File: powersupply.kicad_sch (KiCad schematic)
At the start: 13 parts, among them U1 MAX604

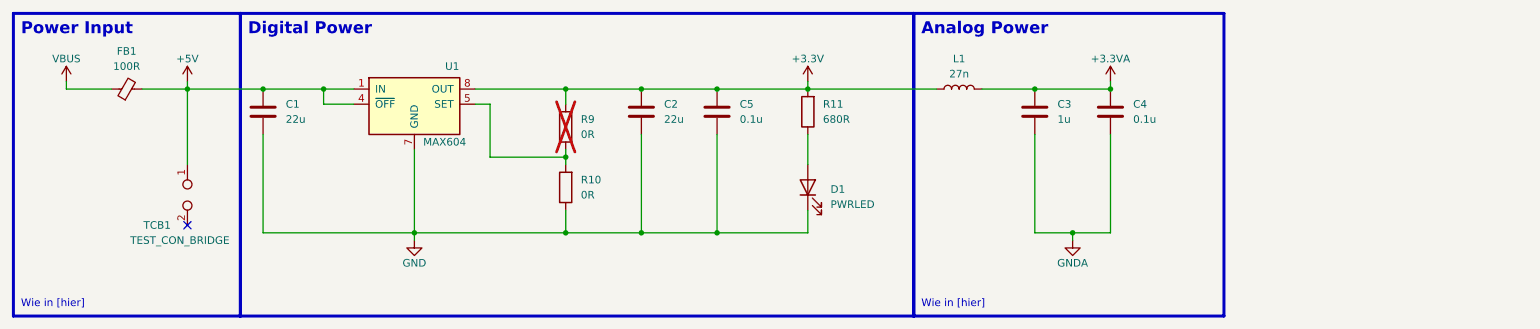
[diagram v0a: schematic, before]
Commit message: Added ESD, updated Footprints, BOM, etc.
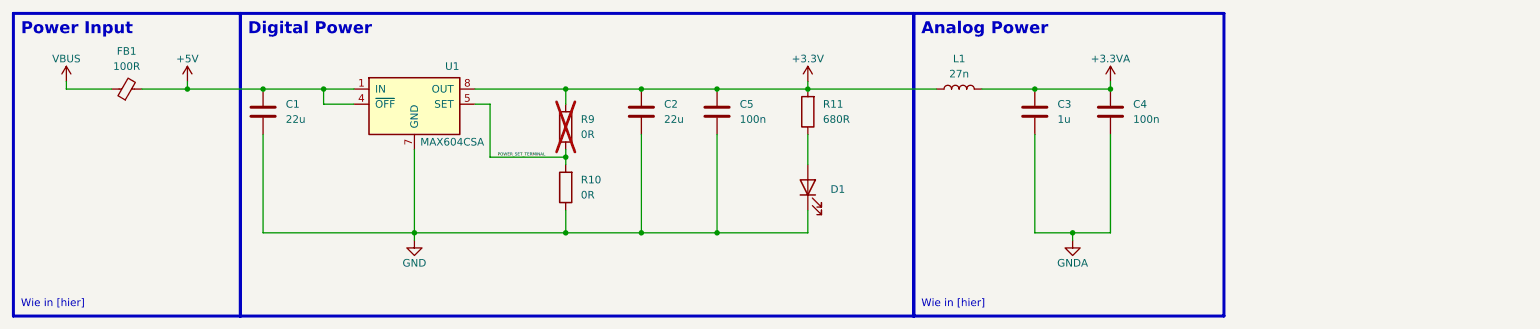
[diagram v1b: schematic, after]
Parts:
- removed TCB1: TEST_CON_BRIDGE, Jumper:SolderJumper-2_P1.3mm_Bridged_Pad1.0x1.5mm, symbol Connector:TestPoint_2Pole
- C4, C5: value 0.1u -> 100n
- D1: value PWRLED -> SML-LX0402UPGC-TR
- U1: value MAX604 -> MAX604CSA
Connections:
- net POWER_SET_TERMINAL: now reaches R10.2, R9.1, U1.5 (SET)
- no-connect marks 1 -> 0
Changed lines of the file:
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@@
   (junction (at 130.81 38.1) (diameter 0) (color 0 0 0 0)
   )
-  (no_connect (at 54.61 60.96))
   (wire (pts (xy 92.71 63.5) (xy 92.71 62.23))
     (stroke (width 0) (type default))
@@
   )
   (wire (pts (xy 54.61 38.1) (xy 67.31 38.1))
-    (stroke (width 0) (type default))
-  )
-  (wire (pts (xy 54.61 38.1) (xy 54.61 50.8))
     (stroke (width 0) (type default))
   )
@@
     (effects (font (size 2 2) (thickness 0.254) bold (color 100 100 100 1)) (justify left bottom))
   )
+  (label "POWER_SET_TERMINAL" (at 106.68 49.53 0) (fields_autoplaced)
+    (effects (font (size 0.5 0.5)) (justify left bottom))
+    (property "Netclass" "Power" (at 106.68 50.03 0)
+      (effects (font (size 0.5 0.5) italic) (justify left))
+    )
+  )
   (symbol (lib_id "Device:C") (at 209.55 41.91 0) (unit 1)
     (in_bom yes) (on_board yes) (dnp no) (fields_autoplaced)
@@
       (effects (font (size 1.27 1.27)) (justify left))
     )
-    (property "Value" "0.1u" (at 213.36 43.18 0)
+    (property "Value" "100n" (at 213.36 43.18 0)
       (effects (font (size 1.27 1.27)) (justify left))
     )
@@
       (effects (font (size 1.27 1.27)) hide)
     )
-    (property "Datasheet" "https://www.mouser.de/datasheet/2/40/AutoMLCCKAM-3216307.pdf" (at 209.55 41.91 0)
+    (property "Datasheet" "~" (at 209.55 41.91 0)
       (effects (font (size 1.27 1.27)) hide)
     )
@@
       (effects (font (size 1.27 1.27)) hide)
     )
-    (property "Datasheet" "https://www.mouser.de/datasheet/2/447/EMI-3217982.pdf" (at 44.45 38.1 0)
+    (property "Datasheet" "~" (at 44.45 38.1 0)
       (effects (font (size 1.27 1.27)) hide)
     )
@@
       (effects (font (size 1.27 1.27)) (justify left))
     )
-    (property "Value" "0.1u" (at 147.32 43.18 0)
+    (property "Value" "100n" (at 147.32 43.18 0)
       (effects (font (size 1.27 1.27)) (justify left))
     )
@@
       (effects (font (size 1.27 1.27)) hide)
     )
-    (property "Datasheet" "https://www.mouser.de/datasheet/2/40/AutoMLCCKAM-3216307.pdf" (at 143.51 41.91 0)
+    (property "Datasheet" "~" (at 143.51 41.91 0)
       (effects (font (size 1.27 1.27)) hide)
     )
@@
       (effects (font (size 1.27 1.27)) hide)
     )
-    (property "Datasheet" "https://www.mouser.de/datasheet/2/40/AutoMLCCKAM-3216307.pdf" (at 67.31 41.91 0)
+    (property "Datasheet" "~" (at 67.31 41.91 0)
       (effects (font (size 1.27 1.27)) hide)
     )
@@
       (effects (font (size 1.27 1.27)) hide)
     )
-    (property "Datasheet" "https://www.mouser.de/datasheet/2/40/AutoMLCCKAM-3216307.pdf" (at 130.81 41.91 0)
+    (property "Datasheet" "~" (at 130.81 41.91 0)
       (effects (font (size 1.27 1.27)) hide)
     )
@@
       (effects (font (size 1.27 1.27)) hide)
     )
-    (property "Datasheet" "https://www.mouser.de/datasheet/2/40/AutoMLCCKAM-3216307.pdf" (at 196.85 41.91 0)
+    (property "Datasheet" "~" (at 196.85 41.91 0)
       (effects (font (size 1.27 1.27)) hide)
     )
@@
       (effects (font (size 1.27 1.27)))
     )
-    (property "Value" "MAX604" (at 97.79 46.99 0)
+    (property "Value" "MAX604CSA" (at 99.06 46.99 0)
       (effects (font (size 1.27 1.27)))
     )
@@
       (effects (font (size 1.27 1.27)) (justify right))
     )
-    (property "Value" "PWRLED" (at 162.56 57.4675 90)
-      (effects (font (size 1.27 1.27)) (justify right))
+    (property "Value" "SML-LX0402UPGC-TR" (at 162.56 57.4675 90)
+      (effects (font (size 1.27 1.27)) (justify right) hide)
     )
     (property "Footprint" "LED_SMD:LED_0402_1005Metric" (at 158.75 54.61 0)
       (effects (font (size 1.27 1.27)) hide)
     )
-    (property "Datasheet" "https://www.mouser.de/datasheet/2/244/LUMX_S_A0003328320_1-2552030.pdf" (at 158.75 54.61 0)
+    (property "Datasheet" "~" (at 158.75 54.61 0)
       (effects (font (size 1.27 1.27)) hide)
     )
@@
         )
       )
-    )
-  )
-  (symbol (lib_id "Connector:TestPoint_2Pole") (at 54.61 55.88 270) (unit 1)
-    (in_bom yes) (on_board yes) (dnp no)
-    (property "Reference" "TCB1" (at 49.53 60.96 90)
-      (effects (font (size 1.27 1.27)))
-    )
-    (property "Value" "TEST_CON_BRIDGE" (at 53.34 63.5 90)
-      (effects (font (size 1.27 1.27)))
-    )
-    (property "Footprint" "Jumper:SolderJumper-2_P1.3mm_Bridged_Pad1.0x1.5mm" (at 54.61 55.88 0)
-      (effects (font (size 1.27 1.27)) hide)
-    )
-    (property "Datasheet" "~" (at 54.61 55.88 0)
-      (effects (font (size 1.27 1.27)) hide)
-    )
-    (pin "1")
-    (pin "2")
-    (instances
-      (project "schneidbrett"
-        (path "/c05974a1-d9e7-44bd-b1f3-81c4ede4353c/86ba3294-cf4a-47ab-b34c-9be2b0ce2123"
-          (reference "TCB1") (unit 1)
-        )
-      )

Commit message: Schematic is done for now, starting layout
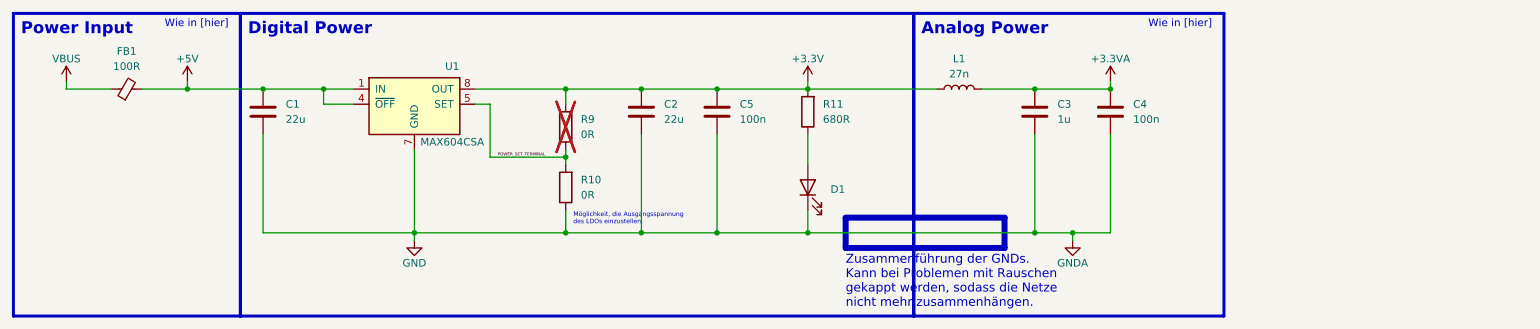
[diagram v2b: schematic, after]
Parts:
- D1: Distributor Link (none) -> https://www.mouser.de/ProductDetail/Lumex/SML-LX0402UPGC-TR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; MFN SML-LX0402UPGC-TR -> (none); Manufacturer (none) -> Lumex; Manufacturer Number (none) -> SML-LX0402UPGC-TR
- FB1: Distributor Link (none) -> https://www.mouser.de/ProductDetail/Pulse-Electronics/BBUP0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; MFN BBUP00321611101Y00 -> (none); Manufacturer (none) -> Pulse Electronics; Manufacturer Number (none) -> BBUP00321611101Y00
- U1: Distributor Link (none) -> https://www.mouser.de/ProductDetail/Analog-Devices-Maxim-In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; MFN MAX604CSA -> (none); Manufacturer (none) -> Analog Devices / Maxim Integrated; Manufacturer Number (none) -> MAX604CSA+
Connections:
- net GNDA is gone; now on net GND: C3.2, C4.2
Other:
- note added: "Möglichkeit, die Ausgangsspannung des LDOs einzustellen."
- note added: "Zusammenführung der GNDs. Kann bei Problemen mit Rauschen gekappt werden, sodass die Netze nicht mehr zusammenhängen."
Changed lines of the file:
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@@
   (junction (at 196.85 38.1) (diameter 0) (color 0 0 0 0)
   )
+  (junction (at 158.75 62.23) (diameter 0) (color 0 0 0 0)
+  )
   (junction (at 77.47 38.1) (diameter 0) (color 0 0 0 0)
   )
@@
   (junction (at 130.81 38.1) (diameter 0) (color 0 0 0 0)
   )
+  (junction (at 196.85 62.23) (diameter 0) (color 0 0 0 0)
+  )
   (wire (pts (xy 92.71 63.5) (xy 92.71 62.23))
     (stroke (width 0) (type default))
@@
   )
   (wire (pts (xy 130.81 38.1) (xy 143.51 38.1))
+    (stroke (width 0) (type default))
+  )
+  (wire (pts (xy 158.75 62.23) (xy 196.85 62.23))
     (stroke (width 0) (type default))
   )
@@
     (fill (type none))
   )
+  (rectangle (start 165.1 59.69) (end 191.77 64.77)
+    (stroke (width 1) (type default) (color 229 0 0 1))
+    (fill (type none))
+  )
   (rectangle (start 176.53 25.4) (end 228.6 76.2)
     (stroke (width 0.5) (type default) (color 100 100 100 1))
     (fill (type none))
   )
-  (text "Wie in [hier]" (at 26.67 74.93 0)
+  (text "Wie in [hier]" (at 50.8 27.94 0)
     (effects (font (size 1.27 1.27)) (justify left bottom) (href "https://youtu.be/wLwKgMBWhpY?t=174"))
   )
-  (text "Wie in [hier]" (at 177.8 74.93 0)
+  (text "Möglichkeit, die Ausgangsspannung\ndes LDOs einzustellen."
+    (at 119.38 60.96 0)
+    (effects (font (size 0.75 0.75) (color 0 0 0 1)) (justify left bottom))
+  )
+  (text "Wie in [hier]" (at 215.9 27.94 0)
     (effects (font (size 1.27 1.27)) (justify left bottom) (href "https://youtu.be/wLwKgMBWhpY?t=214"))
+  )
+  (text "Zusammenführung der GNDs. \nKann bei Problemen mit Rauschen\ngekappt werden, sodass die Netze \nnicht mehr zusammenhängen."
+    (at 165.1 74.93 0)
+    (effects (font (size 1.5 1.5) (color 0 0 0 1)) (justify left bottom))
   )
   (text "Power Input" (at 26.67 29.21 0)
@@
       (effects (font (size 1.27 1.27)) hide)
     )
+    (property "Distributor Link" "" (at 209.55 41.91 0)
+      (effects (font (size 1.27 1.27)) hide)
+    )
+    (property "Manufacturer" "" (at 209.55 41.91 0)
+      (effects (font (size 1.27 1.27)) hide)
+    )
     (pin "1")
     (pin "2")
@@
       (effects (font (size 1.27 1.27)) hide)
     )
-    (property "MFN" "BBUP00321611101Y00" (at 44.45 38.1 90)
+    (property "Manufacturer Number" "BBUP00321611101Y00" (at 44.45 38.1 90)
+      (effects (font (size 1.27 1.27)) hide)
+    )
+    (property "Distributor Link" "https://www.mouser.de/ProductDetail/Pulse-Electronics/BBUP00321611101Y00?qs=rSMjJ%252B1ewcQLINSPAxGW4A%3D%3D" (at 44.45 38.1 0)
+      (effects (font (size 1.27 1.27)) hide)
+    )
+    (property "Manufacturer" "Pulse Electronics" (at 44.45 38.1 0)
       (effects (font (size 1.27 1.27)) hide)
     )
@@
     )
     (property "Datasheet" "~" (at 143.51 41.91 0)
+      (effects (font (size 1.27 1.27)) hide)
+    )
+    (property "Distributor Link" "" (at 143.51 41.91 0)
+      (effects (font (size 1.27 1.27)) hide)
+    )
+    (property "Manufacturer" "" (at 143.51 41.91 0)
       (effects (font (size 1.27 1.27)) hide)
     )
@@
       (effects (font (size 1.27 1.27)) hide)
     )
+    (property "Distributor Link" "" (at 118.11 44.45 0)
+      (effects (font (size 1.27 1.27)) hide)
+    )
+    (property "Manufacturer" "" (at 118.11 44.45 0)
+      (effects (font (size 1.27 1.27)) hide)
+    )
     (pin "1")
     (pin "2")
@@
       (effects (font (size 1.27 1.27)) hide)
     )
+    (property "Distributor Link" "" (at 118.11 54.61 0)
+      (effects (font (size 1.27 1.27)) hide)
+    )
+    (property "Manufacturer" "" (at 118.11 54.61 0)
+      (effects (font (size 1.27 1.27)) hide)
+    )
     (pin "1")
     (pin "2")
@@
       (effects (font (size 1.27 1.27)) hide)
     )
+    (property "Distributor Link" "" (at 67.31 41.91 0)
+      (effects (font (size 1.27 1.27)) hide)
+    )
+    (property "Manufacturer" "" (at 67.31 41.91 0)
+      (effects (font (size 1.27 1.27)) hide)
+    )
     (pin "1")
     (pin "2")
@@
     )
     (property "Datasheet" "~" (at 130.81 41.91 0)
+      (effects (font (size 1.27 1.27)) hide)
+    )
+    (property "Distributor Link" "" (at 130.81 41.91 0)
+      (effects (font (size 1.27 1.27)) hide)
+    )
+    (property "Manufacturer" "" (at 130.81 41.91 0)
       (effects (font (size 1.27 1.27)) hide)
     )
@@
       (effects (font (size 1.27 1.27)) hide)
     )
+    (property "Distributor Link" "" (at 196.85 41.91 0)
+      (effects (font (size 1.27 1.27)) hide)
+    )
+    (property "Manufacturer" "" (at 196.85 41.91 0)
+      (effects (font (size 1.27 1.27)) hide)
+    )
     (pin "1")
     (pin "2")
@@
       (effects (font (size 1.27 1.27)) hide)
     )
-    (property "MFN" "MAX604CSA" (at 92.71 40.64 0)
+    (property "Manufacturer Number" "MAX604CSA+" (at 92.71 40.64 0)
+      (effects (font (size 1.27 1.27)) hide)
+    )
+    (property "Distributor Link" "https://www.mouser.de/ProductDetail/Analog-Devices-Maxim-Integrated/MAX604CSA%2b?qs=1THa7WoU59H7Vh6LHCw%252BVw%3D%3D" (at 92.71 40.64 0)
+      (effects (font (size 1.27 1.27)) hide)
+    )
+    (property "Manufacturer" "Analog Devices / Maxim Integrated" (at 92.71 40.64 0)
       (effects (font (size 1.27 1.27)) hide)
     )
@@
       (effects (font (size 1.27 1.27)) hide)
     )
+    (property "Distributor Link" "" (at 158.75 41.91 0)
+      (effects (font (size 1.27 1.27)) hide)
+    )
+    (property "Manufacturer" "" (at 158.75 41.91 0)
+      (effects (font (size 1.27 1.27)) hide)
+    )
     (pin "1")
     (pin "2")
@@
       (effects (font (size 1.27 1.27)) hide)
     )
-    (property "MFN" "SML-LX0402UPGC-TR" (at 158.75 54.61 90)
+    (property "Manufacturer Number" "SML-LX0402UPGC-TR" (at 158.75 54.61 90)
+      (effects (font (size 1.27 1.27)) hide)
+    )
+    (property "Distributor Link" "https://www.mouser.de/ProductDetail/Lumex/SML-LX0402UPGC-TR?qs=jCymNF74TgVNp7gG86yyZg%3D%3D" (at 158.75 54.61 0)
+      (effects (font (size 1.27 1.27)) hide)
+    )
+    (property "Manufacturer" "Lumex" (at 158.75 54.61 0)
       (effects (font (size 1.27 1.27)) hide)
     )
@@
       (effects (font (size 1.27 1.27)) hide)
     )
+    (property "Distributor Link" "" (at 184.15 38.1 0)
+      (effects (font (size 1.27 1.27)) hide)
+    )
+    (property "Manufacturer" "" (at 184.15 38.1 0)
+      (effects (font (size 1.27 1.27)) hide)
+    )

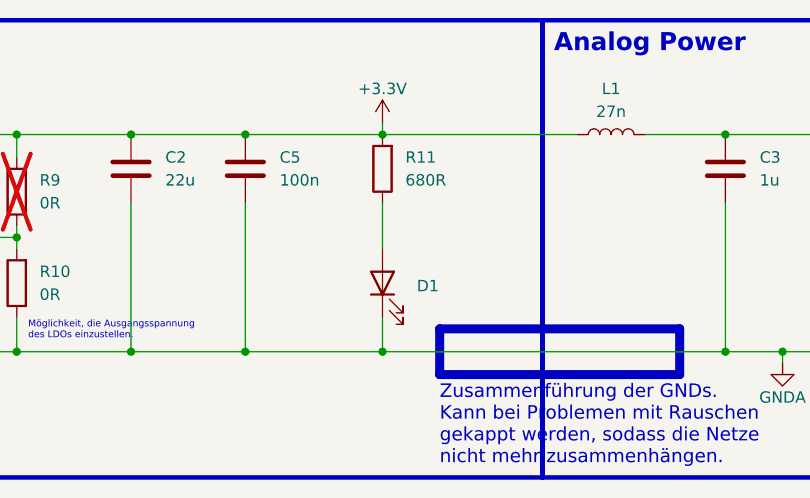
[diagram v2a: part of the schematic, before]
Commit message: Layout done, footprints mostly assigned, 3D models assigned if not annoying to get. Few TODOs left and they are marked on the PCB.
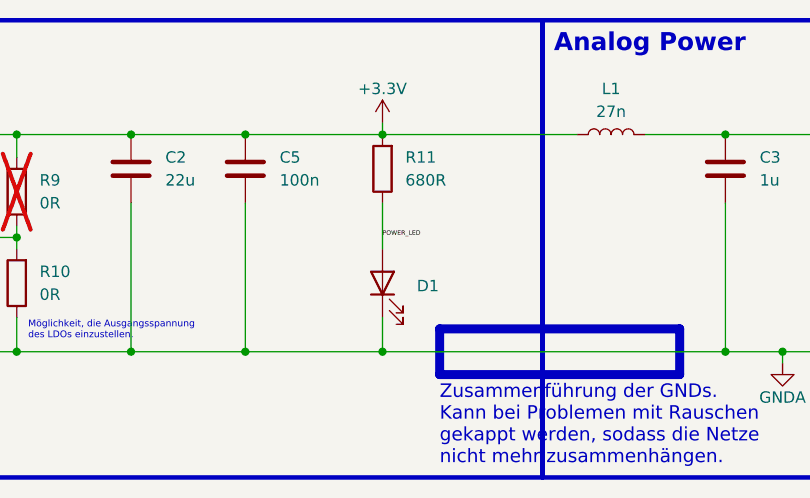
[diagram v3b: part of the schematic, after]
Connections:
- net POWER_LED: now reaches D1.2 (A), R11.1
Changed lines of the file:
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@@
     (effects (font (size 2 2) (thickness 0.254) bold (color 100 100 100 1)) (justify left bottom))
+  )
+  (label "POWER_LED" (at 158.75 49.53 0) (fields_autoplaced)
+    (effects (font (size 0.5 0.5)) (justify left bottom))
+    (property "Netclass" "Power" (at 158.75 50.03 0)
+      (effects (font (size 0.5 0.5) italic) (justify left))
+    )
   )
   (label "POWER_SET_TERMINAL" (at 106.68 49.53 0) (fields_autoplaced)

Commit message: Board outline finished, component placement, added markers, added annotations, etc.
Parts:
- added D12: SML-LX0402UPGC-TR, LED_SMD:LED_0402_1005Metric, symbol Device:LED
- added R2: 680R, Resistor_SMD:R_0402_1005Metric, symbol Device:R
- added TP5: PWR_TP_3V3A, TestPoint:TestPoint_Pad_D1.5mm, symbol Connector:TestPoint
- added TP5: PWR_TP_5V, TestPoint:TestPoint_Pad_D1.5mm, symbol Connector:TestPoint
- added TP5: PWR_TP_GND, TestPoint:TestPoint_Pad_D1.5mm, symbol Connector:TestPoint
- added TP5: PWR_TP_3V3, TestPoint:TestPoint_Pad_D1.5mm, symbol Connector:TestPoint
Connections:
- net +3.3V: now also TP5.1
- net +3.3VA: now also TP5.1
- net +5V: now also R2.2, TP5.1
- net GND: now also D12.1 (K), TP5.1
- net POWER_LED renamed POWER_LED_3V3
- new net POWER_LED_5V: D12.2 (A), R2.1
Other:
- moved on the sheet: C1, C2, C3, C4, C5, D1, FB1, L1, R10, R11, R9, U1

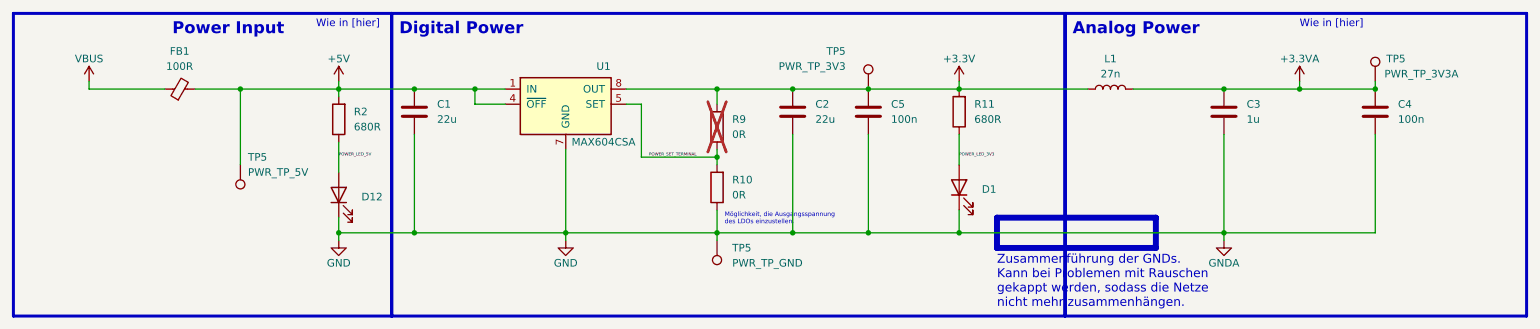
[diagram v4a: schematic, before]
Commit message: Added capacitor voltage rating
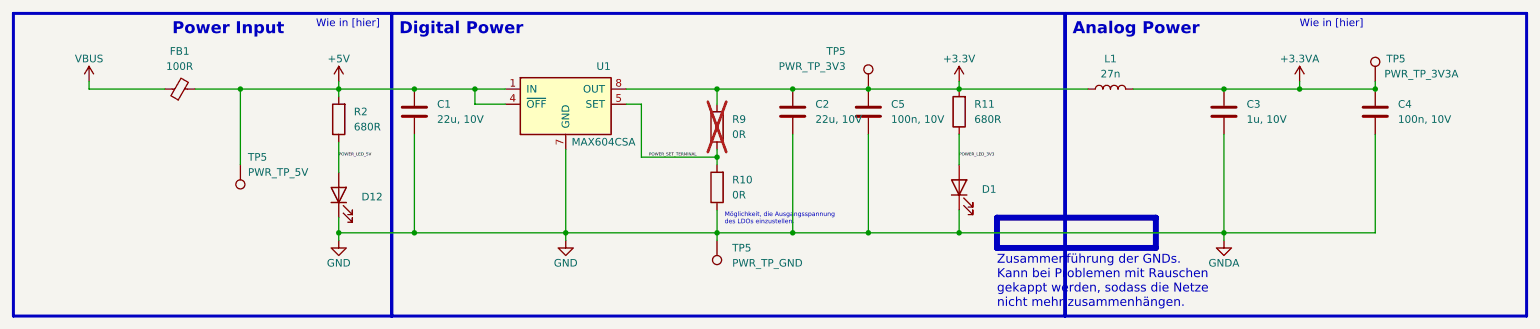
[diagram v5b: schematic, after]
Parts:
- C1, C2: value 22u -> 22u, 10V
- C3: value 1u -> 1u, 10V
- C4, C5: value 100n -> 100n, 10V
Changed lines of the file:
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@@
       (effects (font (size 1.27 1.27)) (justify left))
     )
-    (property "Value" "100n" (at 257.81 43.18 0)
+    (property "Value" "100n, 10V" (at 257.81 43.18 0)
       (effects (font (size 1.27 1.27)) (justify left))
     )
@@
       (effects (font (size 1.27 1.27)) (justify left))
     )
-    (property "Value" "100n" (at 172.72 43.18 0)
+    (property "Value" "100n, 10V" (at 172.72 43.18 0)
       (effects (font (size 1.27 1.27)) (justify left))
     )
@@
       (effects (font (size 1.27 1.27)) (justify left))
     )
-    (property "Value" "22u" (at 96.52 43.18 0)
+    (property "Value" "22u, 10V" (at 96.52 43.18 0)
       (effects (font (size 1.27 1.27)) (justify left))
     )
@@
       (effects (font (size 1.27 1.27)) (justify left))
     )
-    (property "Value" "22u" (at 160.02 43.18 0)
+    (property "Value" "22u, 10V" (at 160.02 43.18 0)
       (effects (font (size 1.27 1.27)) (justify left))
     )
@@
       (effects (font (size 1.27 1.27)) (justify left))
     )
-    (property "Value" "1u" (at 232.41 43.18 0)
-      (effects (font (size 1.27 1.27)) (justify left))
-    )
+    (property "Value" "1u, 10V" (at 232.41 43.18 0)
+      (effects (font (size 1.27 1.27)) (justify left))
+    )
